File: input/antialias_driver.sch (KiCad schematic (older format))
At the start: 20 parts, among them U104 THS4131

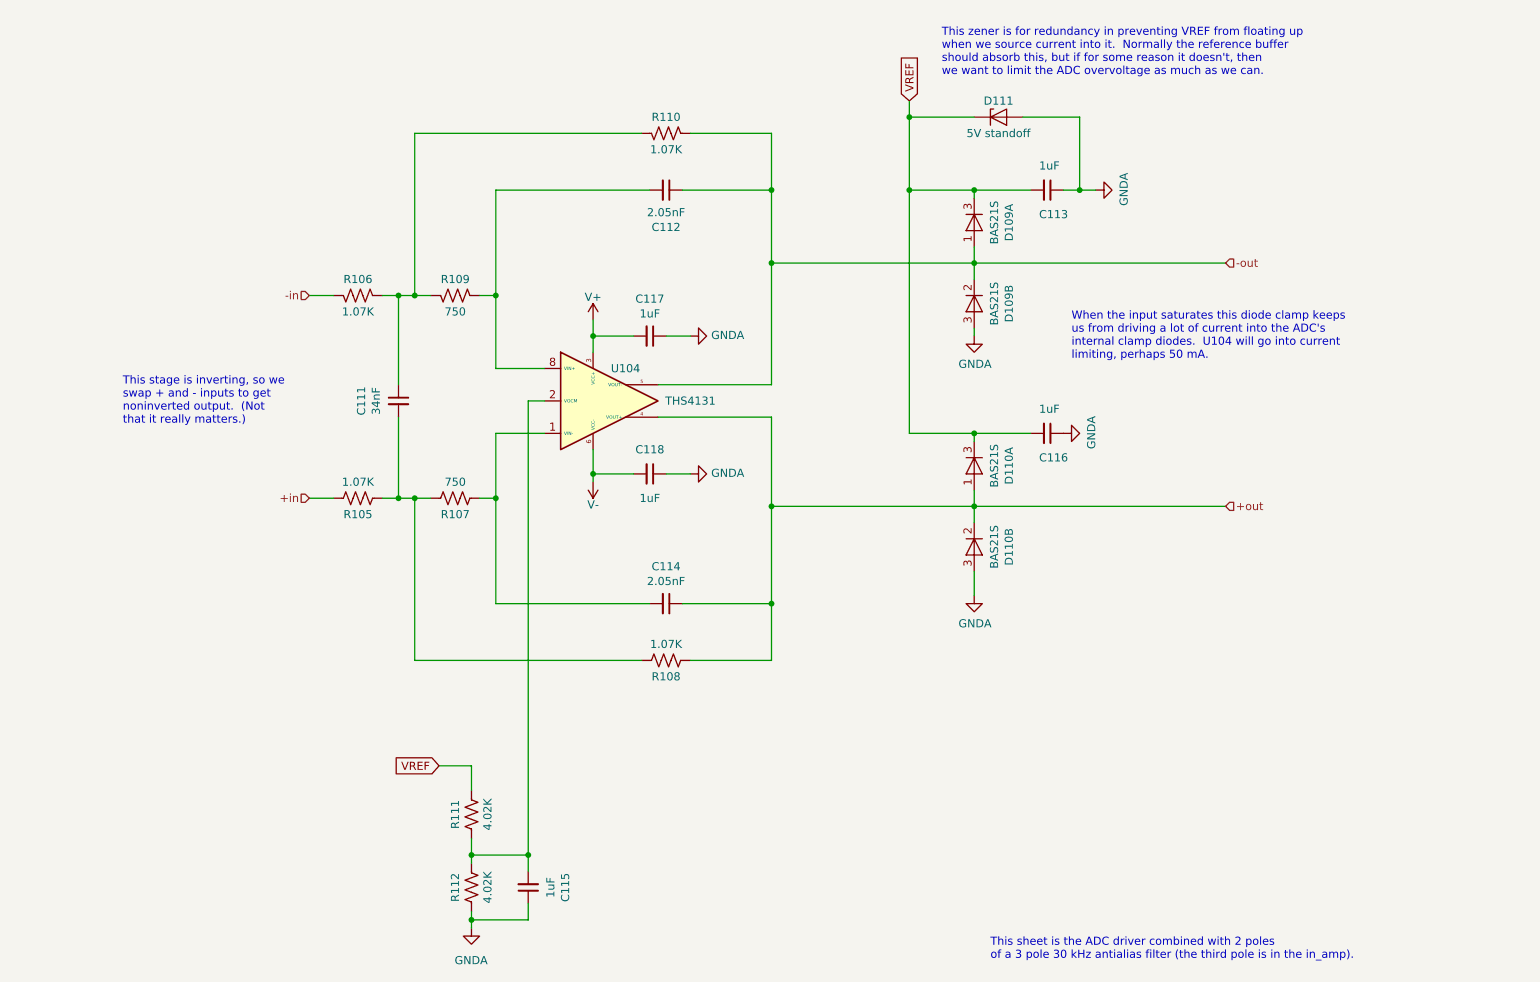
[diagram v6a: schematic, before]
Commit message: Mostly work on power, regulators and distribution.  Also more BOM cleanup.
All of the bypass capacitors are now spec'd and in the DigiKey BOM. TVS zeners are now
spec'd.  Folded together some resistor values and got rid of some 1206 parts that no longer
need that much power rating at the lower supplies.

A affecting all of the input channel sheets is that we now distribute filtered V+, V- and VREF
via sheet ports.  The V+, V- filter is on input_channel.sch and the VREF filter is still in
adc.sch, but is distributed out to the other sheets that need it.

bist_buffer.sch: added buffer for built-in self-test

board_connector.sch: put the input filter for the analog supplies here.

power.sch: added regulators for the supplies.

reference_buffer.sch:
changed components to match those chosen for the V+, V- regulators and added
current steering diodes to bootstrap the reference buffer supply.  This is
necessary because the analog supplies are now derived from VREF.

*.wxsch:
Updates to spice models related to work on supplies.
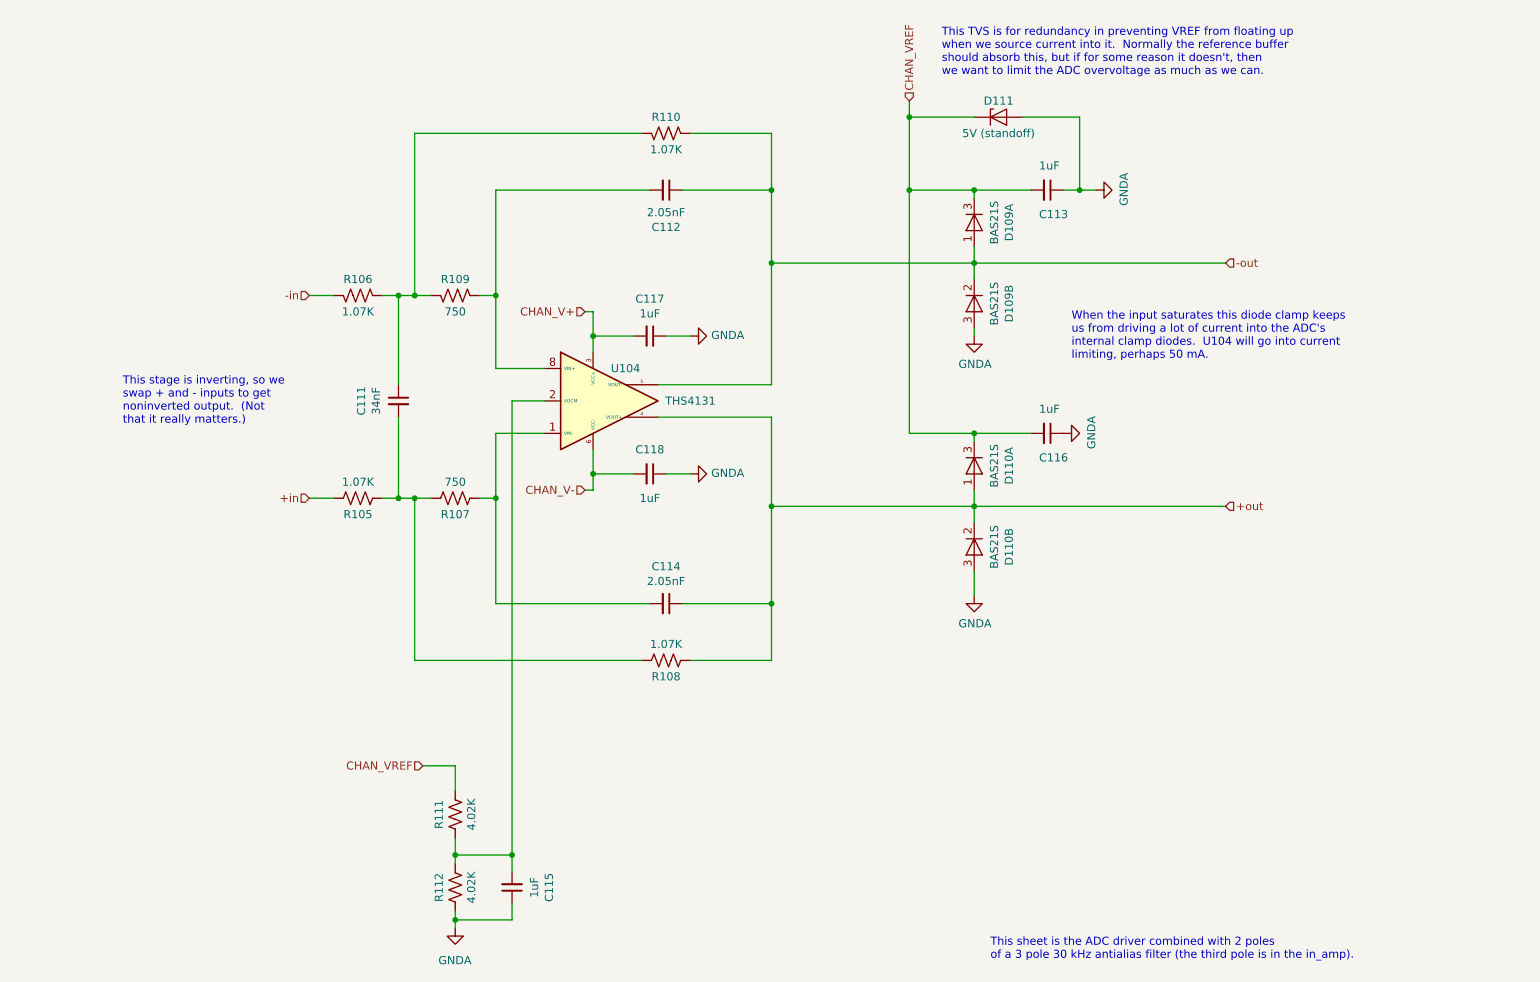
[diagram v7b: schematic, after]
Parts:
- C113, C115, C116, C117, C118: footprint Capacitor_SMD:C_0603_1608Metric -> Capacitor_SMD:C_0805_2012Metric; Description (none) -> CAP CER 1UF 16V X7R 0805; Digikey (none) -> 1276-6471-1-ND; MPN (none) -> CL21B105KOFNNNG
- D111: value 5V standoff -> 5V (standoff); footprint (none) -> Diode_SMD:D_SMA; Description (none) -> TVS DIODE 5V 9.2V DO214AC; Digikey (none) -> 732-9974-1-ND; MPN (none) -> 824500500
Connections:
- net V+ renamed CHAN_V+
- net V- renamed CHAN_V-
- net VREF renamed CHAN_VREF
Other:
- note added: "This TVS is for redundancy in preventing VREF from floating up\nwhen we source current into it. Normally the reference buffer\nshould absorb this, but if for some reason it doesn't, then\nwe want to limit the ADC overvoltage as much as we can."
- note removed: "This zener is for redundancy in preventing VREF from floating up\nwhen we source current into it. Normally the reference buffer\nshould absorb this, but if for some reason it doesn't, then\nwe want to limit the ADC overvoltage as much as we can."
- moved on the sheet: C115, R111, R112
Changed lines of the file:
@@
 EESchema Schematic File Version 4
 LIBS:input_board-cache
-LIBS:input_channel-cache
-LIBS:reference_buffer-cache
 EELAYER 29 0
 EELAYER END
 $Descr A4 11693 8268
 encoding utf-8
-Sheet 4 11
+Sheet 3 12
 Title ""
 Date ""
@@
 Comment4 ""
 $EndDescr
-Wire Wire Line
-	4650 3000 4650 3100
 $Comp
 L Device:C_Small C117
@@
 F 0 "C117" V 4771 3100 50  0000 C CNN
 F 1 "1uF" V 4862 3100 50  0000 C CNN
-F 2 "Capacitor_SMD:C_0603_1608Metric" H 5000 3100 50  0001 C CNN
-F 3 "~" H 5000 3100 50  0001 C CNN
+F 2 "Capacitor_SMD:C_0805_2012Metric" H 5000 3100 50  0001 C CNN
+F 3 "https://media.digikey.com/pdf/Data%20Sheets/Samsung%20PDFs/CL_Series_MLCC_ds.pdf" H 5000 3100 50  0001 C CNN
+F 4 "CAP CER 1UF 16V X7R 0805 " H 5000 3100 50  0001 C CNN "Description"
+F 5 "1276-6471-1-ND" H 5000 3100 50  0001 C CNN "Digikey"
+F 6 "CL21B105KOFNNNG" H 5000 3100 50  0001 C CNN "MPN"
 	1    5000 3100
 	0    1    1    0
@@
 L Device:R_US R111
 U 1 1 5E1955AB
-P 3900 6050
-F 0 "R111" V 4000 6050 50  0000 C CNN
-F 1 "4.02K" V 3800 6050 50  0000 C CNN
-F 2 "Resistor_SMD:R_0805_2012Metric" V 3940 6040 50  0001 C CNN
-F 3 "~" H 3900 6050 50  0001 C CNN
-F 4 "0.1%" H 3900 6050 50  0001 C CNN "Notes"
-	1    3900 6050
+P 3800 6050
+F 0 "R111" V 3900 6050 50  0000 C CNN
+F 1 "4.02K" V 3700 6050 50  0000 C CNN
+F 2 "Resistor_SMD:R_0805_2012Metric" V 3840 6040 50  0001 C CNN
+F 3 "~" H 3800 6050 50  0001 C CNN
+F 4 "0.1%" H 3800 6050 50  0001 C CNN "Notes"
+	1    3800 6050
 	-1   0    0    1
 $EndComp
@@
 L Device:R_US R112
 U 1 1 5E1955AC
-P 3900 6500
-F 0 "R112" V 4000 6500 50  0000 C CNN
-F 1 "4.02K" V 3800 6500 50  0000 C CNN
-F 2 "Resistor_SMD:R_0805_2012Metric" V 3940 6490 50  0001 C CNN
-F 3 "~" H 3900 6500 50  0001 C CNN
-F 4 "0.1%" H 3900 6500 50  0001 C CNN "Notes"
-	1    3900 6500
+P 3800 6500
+F 0 "R112" V 3900 6500 50  0000 C CNN
+F 1 "4.02K" V 3700 6500 50  0000 C CNN
+F 2 "Resistor_SMD:R_0805_2012Metric" V 3840 6490 50  0001 C CNN
+F 3 "~" H 3800 6500 50  0001 C CNN
+F 4 "0.1%" H 3800 6500 50  0001 C CNN "Notes"
+	1    3800 6500
 	-1   0    0    1
 $EndComp
@@
 L power:GNDA #PWR0120
 U 1 1 5E1955AD
-P 3900 6750
-F 0 "#PWR0120" H 3900 6500 50  0001 C CNN
-F 1 "GNDA" H 4000 6550 50  0000 R CNN
-F 2 "" H 3900 6750 50  0001 C CNN
-F 3 "" H 3900 6750 50  0001 C CNN
-	1    3900 6750
+P 3800 6750
+F 0 "#PWR0120" H 3800 6500 50  0001 C CNN
+F 1 "GNDA" H 3900 6550 50  0000 R CNN
+F 2 "" H 3800 6750 50  0001 C CNN
+F 3 "" H 3800 6750 50  0001 C CNN
+	1    3800 6750
 	1    0    0    -1
 $EndComp
-Text GLabel 3700 5750 0    50   Input ~ 0
-VREF
-Wire Wire Line
-	3700 5750 3900 5750
-Wire Wire Line
-	3900 5750 3900 5900
-Connection ~ 3900 6300
-Wire Wire Line
-	3900 6300 3900 6200
-Wire Wire Line
-	3900 6650 3900 6700
-Wire Wire Line
-	3900 6300 3900 6350
+Wire Wire Line
+	3800 5750 3800 5900
+Connection ~ 3800 6300
+Wire Wire Line
+	3800 6300 3800 6200
+Wire Wire Line
+	3800 6650 3800 6700
+Wire Wire Line
+	3800 6300 3800 6350
 $Comp
 L Device:C_Small C115
 U 1 1 5E1955AE
-P 4250 6500
-F 0 "C115" V 4021 6500 50  0000 C CNN
-F 1 "1uF" V 4112 6500 50  0000 C CNN
-F 2 "Capacitor_SMD:C_0603_1608Metric" H 4250 6500 50  0001 C CNN
-F 3 "~" H 4250 6500 50  0001 C CNN
-	1    4250 6500
+P 4150 6500
+F 0 "C115" V 3921 6500 50  0000 C CNN
+F 1 "1uF" V 4012 6500 50  0000 C CNN
+F 2 "Capacitor_SMD:C_0805_2012Metric" H 4150 6500 50  0001 C CNN
+F 3 "https://media.digikey.com/pdf/Data%20Sheets/Samsung%20PDFs/CL_Series_MLCC_ds.pdf" H 4150 6500 50  0001 C CNN
+F 4 "CAP CER 1UF 16V X7R 0805 " H 4150 6500 50  0001 C CNN "Description"
+F 5 "1276-6471-1-ND" H 4150 6500 50  0001 C CNN "Digikey"
+F 6 "CL21B105KOFNNNG" H 4150 6500 50  0001 C CNN "MPN"
+	1    4150 6500
 	-1   0    0    1
 $EndComp
 Wire Wire Line
-	4250 6400 4250 6300
-Wire Wire Line
-	3900 6700 4250 6700
-Wire Wire Line
-	4250 6600 4250 6700
-Connection ~ 3900 6700
-Wire Wire Line
-	3900 6700 3900 6750
+	4150 6400 4150 6300
+Wire Wire Line
+	3800 6700 4150 6700
+Wire Wire Line
+	4150 6600 4150 6700
+Connection ~ 3800 6700
+Wire Wire Line
+	3800 6700 3800 6750
 Wire Wire Line
 	4650 3800 4650 3950
@@
 F 0 "C118" V 4850 3950 50  0000 C CNN
 F 1 "1uF" V 5150 3950 50  0000 C CNN
-F 2 "Capacitor_SMD:C_0603_1608Metric" H 5000 3950 50  0001 C CNN
-F 3 "~" H 5000 3950 50  0001 C CNN
+F 2 "Capacitor_SMD:C_0805_2012Metric" H 5000 3950 50  0001 C CNN
+F 3 "https://media.digikey.com/pdf/Data%20Sheets/Samsung%20PDFs/CL_Series_MLCC_ds.pdf" H 5000 3950 50  0001 C CNN
+F 4 "CAP CER 1UF 16V X7R 0805 " H 5000 3950 50  0001 C CNN "Description"
+F 5 "1276-6471-1-ND" H 5000 3950 50  0001 C CNN "Digikey"
+F 6 "CL21B105KOFNNNG" H 5000 3950 50  0001 C CNN "MPN"
 	1    5000 3950
 	0    1    1    0
@@
 Wire Wire Line
 	5100 3950 5250 3950
-Wire Wire Line
-	4650 4000 4650 3950
 Connection ~ 4650 3950
 Wire Wire Line
@@
 This sheet is the ADC driver combined with 2 poles \nof a 3 pole 30 kHz antialias filter (the third pole is in the in_amp).\n
 Wire Wire Line
-	3900 6300 4250 6300
+	3800 6300 4150 6300
 Wire Wire Line
 	3950 4100 4050 4100
@@
 	5750 5100 5750 4750
 Wire Wire Line
-	4250 6300 4250 3500
-Connection ~ 4250 6300
-Wire Wire Line
-	4250 3500 4350 3500
+	4150 6300 4150 3500
+Connection ~ 4150 6300
 Wire Wire Line
 	3550 5100 4950 5100
@@
 F 0 "C113" V 7600 2150 50  0000 L CNN
 F 1 "1uF" V 7300 2150 50  0000 L CNN
-F 2 "Capacitor_SMD:C_0603_1608Metric" H 7450 2200 50  0001 C CNN
-F 3 "~" H 7450 2200 50  0001 C CNN
+F 2 "Capacitor_SMD:C_0805_2012Metric" H 7450 2200 50  0001 C CNN
+F 3 "https://media.digikey.com/pdf/Data%20Sheets/Samsung%20PDFs/CL_Series_MLCC_ds.pdf" H 7450 2200 50  0001 C CNN
+F 4 "CAP CER 1UF 16V X7R 0805 " H 7450 2200 50  0001 C CNN "Description"
+F 5 "1276-6471-1-ND" H 7450 2200 50  0001 C CNN "Digikey"
+F 6 "CL21B105KOFNNNG" H 7450 2200 50  0001 C CNN "MPN"
 	1    7450 2200
 	0    1    1    0
@@
 F 0 "C116" V 7600 3650 50  0000 L CNN
 F 1 "1uF" V 7300 3650 50  0000 L CNN
-F 2 "Capacitor_SMD:C_0603_1608Metric" H 7450 3700 50  0001 C CNN
-F 3 "~" H 7450 3700 50  0001 C CNN
+F 2 "Capacitor_SMD:C_0805_2012Metric" H 7450 3700 50  0001 C CNN
+F 3 "https://media.digikey.com/pdf/Data%20Sheets/Samsung%20PDFs/CL_Series_MLCC_ds.pdf" H 7450 3700 50  0001 C CNN
+F 4 "CAP CER 1UF 16V X7R 0805 " H 7450 3700 50  0001 C CNN "Description"
+F 5 "1276-6471-1-ND" H 7450 3700 50  0001 C CNN "Digikey"
+F 6 "CL21B105KOFNNNG" H 7450 3700 50  0001 C CNN "MPN"
 	1    7450 3700
 	0    1    1    0
@@
 Wire Wire Line
 	7000 3700 7000 3750
-Text GLabel 6600 1650 1    50   Input ~ 0
-VREF
 Wire Wire Line
 	5750 3600 5750 4150
@@
 Wire Wire Line
 	5750 2650 5750 3400
-$Comp
-L Device:D_Zener D111
-U 1 1 5E40EE20
-P 7150 1750
-F 0 "D111" H 7150 1850 50  0000 C CNN
-F 1 "5V standoff" H 7150 1650 50  0000 C CNN
-F 2 "" H 7150 1750 50  0001 C CNN
-F 3 "~" H 7150 1750 50  0001 C CNN
-	1    7150 1750
-	1    0    0    -1
-$EndComp
 Wire Wire Line
 	6600 3700 7000 3700
@@
 When the input saturates this diode clamp keeps \nus from driving a lot of current into the ADC's \ninternal clamp diodes.  U104 will go into current\nlimiting, perhaps 50 mA.
 Text Notes 6800 1500 0    50   ~ 0
-This zener is for redundancy in preventing VREF from floating up\nwhen we source current into it.  Normally the reference buffer\nshould absorb this, but if for some reason it doesn't, then\nwe want to limit the ADC overvoltage as much as we can.
+This TVS is for redundancy in preventing VREF from floating up\nwhen we source current into it.  Normally the reference buffer\nshould absorb this, but if for some reason it doesn't, then\nwe want to limit the ADC overvoltage as much as we can.
 Text Notes 1750 3650 0    50   ~ 0
 This stage is inverting, so we \nswap + and - inputs to get\nnoninverted output.  (Not \nthat it really matters.)
-$Comp
-L ilemt_input:V+ #PWR0119
-U 1 1 5E50E0CF
-P 4650 3000
-F 0 "#PWR0119" H 4650 2850 50  0001 C CNN
-F 1 "V+" H 4650 3140 50  0000 C CNN
-F 2 "" H 4650 3000 50  0001 C CNN
-F 3 "" H 4650 3000 50  0001 C CNN
-	1    4650 3000
+Text HLabel 4600 2950 0    50   Input ~ 0
+CHAN_V+
+Text HLabel 4600 4050 0    50   Input ~ 0
+CHAN_V-
+Wire Wire Line
+	4600 2950 4650 2950
+Wire Wire Line
+	4650 2950 4650 3100
+Wire Wire Line
+	4600 4050 4650 4050
+Wire Wire Line
+	4650 3950 4650 4050
+Wire Wire Line
+	4150 3500 4350 3500
+$Comp
+L Device:D_Zener D?
+U 1 1 5E341688
+P 7150 1750
+AR Path="/5E51E83D/5E341688" Ref="D?"  Part="1"
+AR Path="/5DFCF14D/5DE6CDF8/5E341688" Ref="D111"  Part="1"
+F 0 "D111" H 7150 1850 50  0000 C CNN
+F 1 "5V (standoff)" H 7150 1650 50  0000 C CNN
+F 2 "Diode_SMD:D_SMA" H 7150 1750 50  0001 C CNN
+F 3 "https://katalog.we-online.de/pbs/datasheet/824500500.pdf" H 7150 1750 50  0001 C CNN
+F 4 "824500500" H 7150 1750 50  0001 C CNN "MPN"
+F 5 "TVS DIODE 5V 9.2V DO214AC" H 7150 1750 50  0001 C CNN "Description"
+F 6 "732-9974-1-ND" H 7150 1750 50  0001 C CNN "Digikey"
+	1    7150 1750
 	1    0    0    -1
 $EndComp
-$Comp
-L ilemt_input:V- #PWR0121
-U 1 1 5E50E68B
-P 4650 4100
-F 0 "#PWR0121" H 4650 3950 50  0001 C CNN
-F 1 "V-" H 4650 4060 50  0000 C CNN
-F 2 "" H 4650 4200 50  0001 C CNN
-F 3 "" H 4650 4200 50  0001 C CNN
-	1    4650 4100
-	1    0    0    -1
-$EndComp
+Text HLabel 6600 1650 1    50   Input ~ 0
+CHAN_VREF
+Text HLabel 3600 5750 0    50   Input ~ 0
+CHAN_VREF
+Wire Wire Line
+	3600 5750 3800 5750
 $EndSCHEMATC
